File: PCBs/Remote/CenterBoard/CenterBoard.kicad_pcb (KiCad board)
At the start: 4 copper layers, 100 x 100 mm, 76 parts, among them J201 DX07S016JA1R1500, J401 SMA, J501 Conn_01x11, U201 LPC51U68JBD64, U202 W25Q128JVS, U301 SC189ZSKTRT, U401 nRF24L01P, U402 RFX2401C, U601 Joystick Left, U602 Joystick Right, X401 16MHz

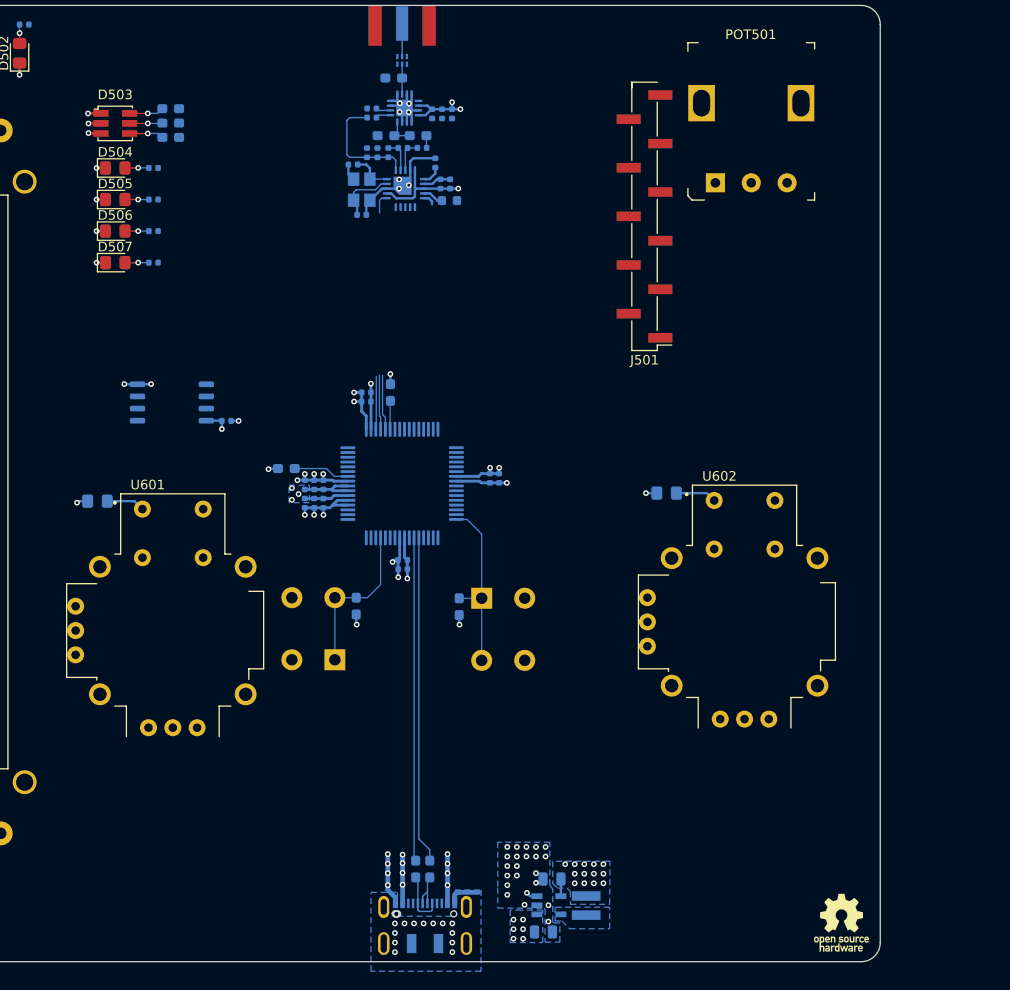
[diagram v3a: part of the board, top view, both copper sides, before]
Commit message: Made the keyboard PCB. With LPC software started pin assignment on the LPC
Signed-off-by: Eldalote.Electronics <Eldalote.Electronics@gmail.com>
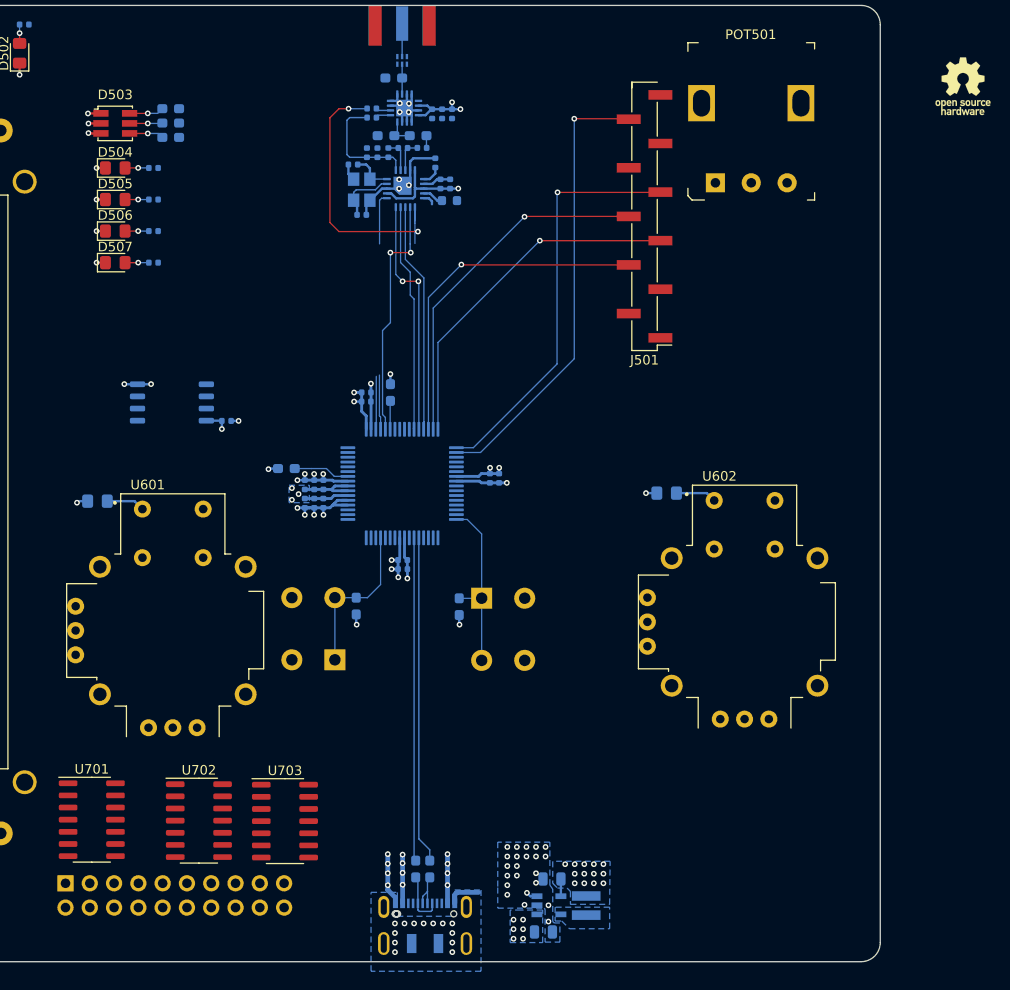
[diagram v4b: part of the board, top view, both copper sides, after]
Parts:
- added J701: Conn_02x10_Odd_Even, Connector_PinHeader_2.54mm:PinHeader_2x10_P2.54mm_Vertical, B.Cu at (114.8, 151.8)
- added U701: 74HC14, Package_SO:SOIC-14_3.9x8.7mm_P1.27mm, F.Cu at (117.5, 145.2)
- added U702: 74HC14, Package_SO:SOIC-14_3.9x8.7mm_P1.27mm, F.Cu at (128.8, 145.2)
- added U703: 74HC14, Package_SO:SOIC-14_3.9x8.7mm_P1.27mm, F.Cu at (137.8, 145.3)
- moved LOGO101 88.4 mm to (208.7, 68.5)
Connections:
- U201 pad 37: Net-(U201-Pad37) -> nRF_CSn
- U201 pad 43: Net-(U201-Pad43) -> nRF_MOSI
- U201 pad 44: Net-(U201-Pad44) -> nRF_MISO
- U201 pad 45: Net-(U201-Pad45) -> nRF_SCLK
- U201 pad 46: Net-(U201-Pad46) -> Screen_SPI_SCLK
- U201 pad 47: Net-(U201-Pad47) -> Screen_SPI_MOSI
- U201 pad 48: Net-(U201-Pad48) -> Screen_SPI_MISO
- U201 pad 49: Net-(U201-Pad49) -> Screen_SPI_CSn_TFT
- U201 pad 50: Net-(U201-Pad50) -> Screen_SPI_CSn_SDCard
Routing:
- net Screen_SPI_CSn_SDCard: track 0.00 -> 47.2 mm, vias 0 -> 1
- net Screen_SPI_CSn_TFT: track 0.00 -> 42.9 mm, vias 0 -> 1
- net Screen_SPI_MOSI: track 0.00 -> 37.1 mm, vias 0 -> 1
- net Screen_SPI_MISO: track 0.00 -> 36.7 mm, vias 0 -> 1
- net Screen_SPI_SCLK: track 0.00 -> 36.2 mm, vias 0 -> 1
- net nRF_CE: track 0.00 -> 30.5 mm, vias 0 -> 2
- net nRF_CSn: track 0.00 -> 25.8 mm, vias 0 -> 2
- net nRF_MISO: track 0.00 -> 25.2 mm, vias 0 -> 2
- net nRF_SCLK: track 0.00 -> 24.0 mm
- net nRF_MOSI: track 0.00 -> 23.9 mm
- net Net-(U201-Pad37): track 5.77 -> 0.00 mm
- net nRF_IRQ: track 2.18 -> 5.41 mm
- net GND: track 87.2 -> 89.1 mm, vias 70 -> 72

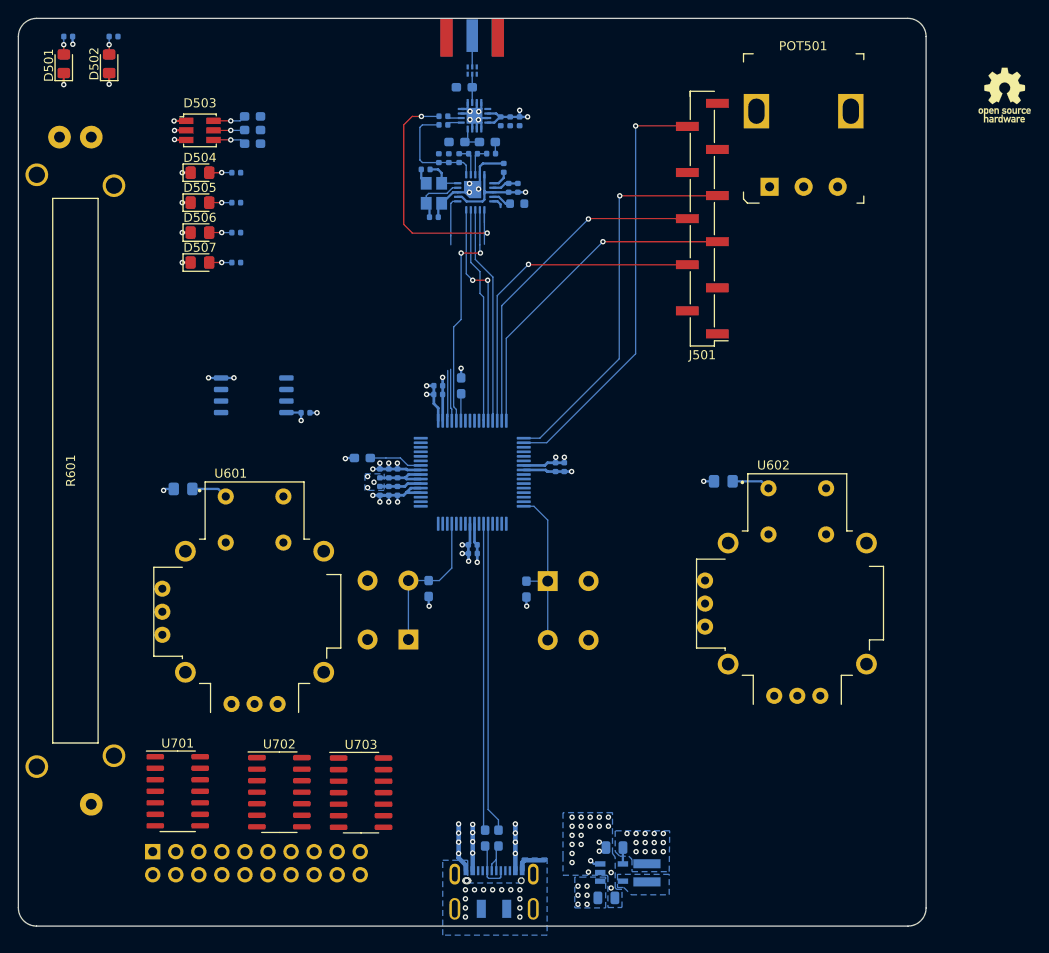
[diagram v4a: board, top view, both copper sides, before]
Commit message: Screen POT->PWM and RGB LEDS reworked, making space on the CPU pins. Almost done
Signed-off-by: Eldalote.Electronics <Eldalote.Electronics@gmail.com>
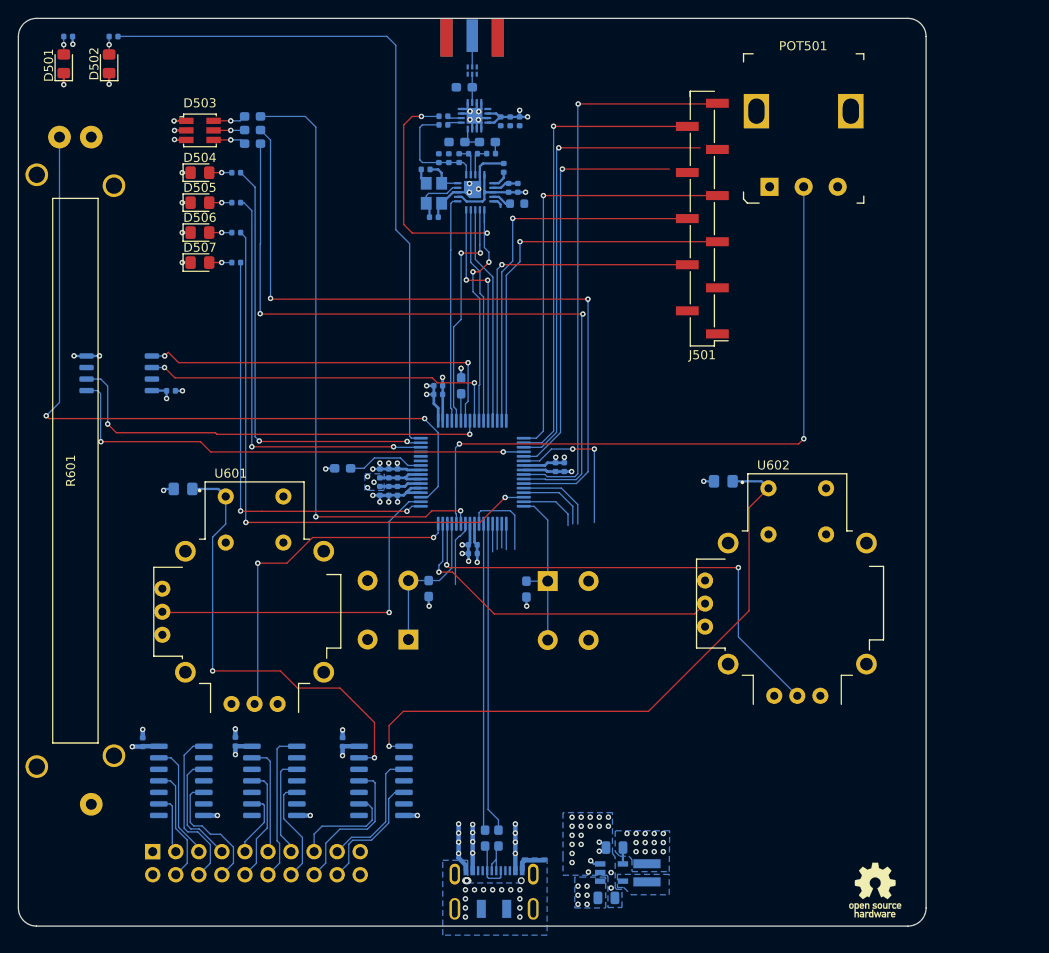
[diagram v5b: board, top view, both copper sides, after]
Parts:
- added C701: 100nF, Capacitor_SMD:C_0402_1005Metric, B.Cu at (123.9, 139.7)
- added C702: 100nF, Capacitor_SMD:C_0402_1005Metric, B.Cu at (135.7, 139.7)
- added C703: 100nF, Capacitor_SMD:C_0402_1005Metric, B.Cu at (113.7, 139.7)
- U701, U702, U703: moved to B.Cu
- moved LOGO101 88.7 mm to (194.4, 156.0)
- moved U202 15.0 mm to (111.1, 99.1)
- moved C214 15.0 mm to (116.8, 101.0)
- moved U703 2.60 mm to (140.0, 144.0), turned to 180 degrees
- moved R206 2.45 mm to (135.7, 109.6)
- moved U702 1.37 mm to (128.2, 144.0), turned to 180 degrees
- moved U701 1.22 mm to (118.0, 144.0), turned to 180 degrees
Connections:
- J501 pad 1: /LEDs and Screen/Vin -> +3V3
- U201 pad 11: Net-(U201-Pad11) -> LED_USER_RGB_B
- U201 pad 12: Net-(U201-Pad12) -> Screen_Backlight_pot
- U201 pad 14: Net-(U201-Pad14) -> JS_right_H
- U201 pad 15: Net-(U201-Pad15) -> JS_right_V
- U201 pad 16: Net-(U201-Pad16) -> JS_left_H
- U201 pad 17: Net-(U201-Pad17) -> USER_LED_3
- U201 pad 18: Net-(U201-Pad18) -> JS_left_V
- U201 pad 19: Net-(U201-Pad19) -> Throttle
- U201 pad 30: Net-(U201-Pad30) -> USER_LED_1
- U201 pad 31: Net-(U201-Pad31) -> USER_LED_0
- U201 pad 32: Net-(U201-Pad32) -> LED_ERROR
- U201 pad 36: Net-(U201-Pad36) -> nRF_IRQ
- U201 pad 39: Net-(U201-Pad39) -> /LPC51/Flash_SPI_MOSI
- U201 pad 40: Net-(U201-Pad40) -> /LPC51/Flash_SPI_MISO
- U201 pad 41: Net-(U201-Pad41) -> /LPC51/Flash_SPI_SCLK
- U201 pad 42: Net-(U201-Pad42) -> nRF_CE
- U201 pad 52: Net-(U201-Pad52) -> /LPC51/Flash_SPI_CSn
- U201 pad 57: Net-(U201-Pad57) -> Screen_Backlight_PWM
- U201 pad 58: Net-(U201-Pad58) -> LED_USER_RGB_R
- U201 pad 59: Net-(U201-Pad59) -> LED_USER_RGB_G
- U201 pad 62: Net-(U201-Pad62) -> USER_LED_2
- U701 pad 1: Net-(U701-Pad1) -> /Keyboard connector and Schmitt triggers/SW_0
- U701 pad 11: Net-(U701-Pad11) -> /Keyboard connector and Schmitt triggers/SW_4
- U701 pad 13: Net-(U701-Pad13) -> /Keyboard connector and Schmitt triggers/SW_1
- U701 pad 14: Net-(U701-Pad14) -> +3V3
- U701 pad 3: Net-(U701-Pad3) -> /Keyboard connector and Schmitt triggers/SW_5
- U701 pad 5: Net-(U701-Pad5) -> /Keyboard connector and Schmitt triggers/SW_8
- U701 pad 7: Net-(U701-Pad7) -> GND
- U701 pad 9: Net-(U701-Pad9) -> /Keyboard connector and Schmitt triggers/SW_7
- U702 pad 1: Net-(U702-Pad1) -> /Keyboard connector and Schmitt triggers/SW_9
- U702 pad 11: Net-(U702-Pad11) -> /Keyboard connector and Schmitt triggers/SW_2
- U702 pad 13: Net-(U702-Pad13) -> /Keyboard connector and Schmitt triggers/SW_6
- U702 pad 14: Net-(U702-Pad14) -> +3V3
- U702 pad 3: Net-(U702-Pad3) -> /Keyboard connector and Schmitt triggers/SW_Enter
- U702 pad 5: Net-(U702-Pad5) -> /Keyboard connector and Schmitt triggers/SW_3
- U702 pad 7: Net-(U702-Pad7) -> GND
- U702 pad 9: Net-(U702-Pad9) -> /Keyboard connector and Schmitt triggers/SW_point
- U703 pad 1: Net-(U703-Pad1) -> JS_right_button
- U703 pad 11: Net-(U703-Pad11) -> /Keyboard connector and Schmitt triggers/SW_M0
- U703 pad 13: Net-(U703-Pad13) -> JS_left_button
- U703 pad 14: Net-(U703-Pad14) -> +3V3
- U703 pad 3: Net-(U703-Pad3) -> /Keyboard connector and Schmitt triggers/SW_M2
- U703 pad 5: Net-(U703-Pad5) -> /Keyboard connector and Schmitt triggers/SW_M1
- U703 pad 7: Net-(U703-Pad7) -> GND
- U703 pad 9: Net-(U703-Pad9) -> /Keyboard connector and Schmitt triggers/SW_M3
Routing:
- net Throttle: track 0.00 -> 83.6 mm, vias 0 -> 2
- net LED_USER_RGB_G: track 0.00 -> 80.7 mm, vias 0 -> 2
- net LED_USER_RGB_R: track 0.00 -> 78.7 mm, vias 0 -> 2
- net LED_ERROR: track 0.00 -> 76.1 mm
- net Screen_Backlight_pot: track 0.00 -> 75.0 mm, vias 0 -> 2
- net LED_USER_RGB_B: track 0.00 -> 67.2 mm, vias 0 -> 2
- net USER_LED_2: track 0.00 -> 63.9 mm, vias 0 -> 2
- net JS_right_button: track 4.27 -> 67.5 mm, vias 0 -> 1
- net Screen_Backlight_PWM: track 0.00 -> 62.3 mm, vias 0 -> 1
- net /LPC51/Flash_SPI_CSn: track 0.00 -> 54.1 mm, vias 0 -> 2
- net JS_right_H: track 0.00 -> 53.6 mm, vias 0 -> 2
- net Net-(U201-Pad51): track 0.00 -> 51.3 mm, vias 0 -> 1
- net /LPC51/Flash_SPI_MISO: track 0.00 -> 48.7 mm, vias 0 -> 2
- net USER_LED_0: track 0.00 -> 48.3 mm, vias 0 -> 2
- net USER_LED_3: track 0.00 -> 47.5 mm, vias 0 -> 2
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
